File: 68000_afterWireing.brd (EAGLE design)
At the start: 100 x 80 mm, 19 parts, among them IC1 74LS32N, IC2 74LS04N, IC3 74LS04N, X1 22-23-2021

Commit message: Fixed errors and warnings after first autoroute. But Need to move components because their are still airwires after autorouting
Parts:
- removed CLK_OSCILLATOR: ASE, crystal:ASE
- added QG1: SG-615PTW, crystal:SG-615
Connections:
- removed net VSS: 6821_IO.1
- net GND: now also 6821_IO.1, QG1.2; no longer CLK_OSCILLATOR.2
- net N$10: now also MC68000.10
- net N$16: now also D1.A
- net N$26: now also QG1.3
- net N$6: now also 6821_IO.25
- net VCC: now also QG1.4; no longer CLK_OSCILLATOR.4
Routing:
- net GND: track 0.00 -> 343.4 mm, vias 0 -> 9
- net VCC: track 0.00 -> 338.3 mm, vias 0 -> 3
- net A10: track 0.00 -> 207.1 mm, vias 0 -> 8
- net A5: track 0.00 -> 203.2 mm, vias 0 -> 10
- net A9: track 0.00 -> 185.3 mm, vias 0 -> 10
- net D2: track 0.00 -> 184.7 mm, vias 0 -> 5
- net D0: track 0.00 -> 178.2 mm, vias 0 -> 5
- net D1: track 0.00 -> 173.3 mm, vias 0 -> 3
- net A1: track 0.00 -> 171.0 mm, vias 0 -> 5
- net D4: track 0.00 -> 170.2 mm, vias 0 -> 7
- net D5: track 0.00 -> 169.9 mm, vias 0 -> 5
- net A11: track 0.00 -> 166.9 mm, vias 0 -> 10
- net A7: track 0.00 -> 153.5 mm, vias 0 -> 6
- net N$22: track 0.00 -> 150.2 mm, vias 0 -> 4
- net A2: track 0.00 -> 148.7 mm, vias 0 -> 7
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
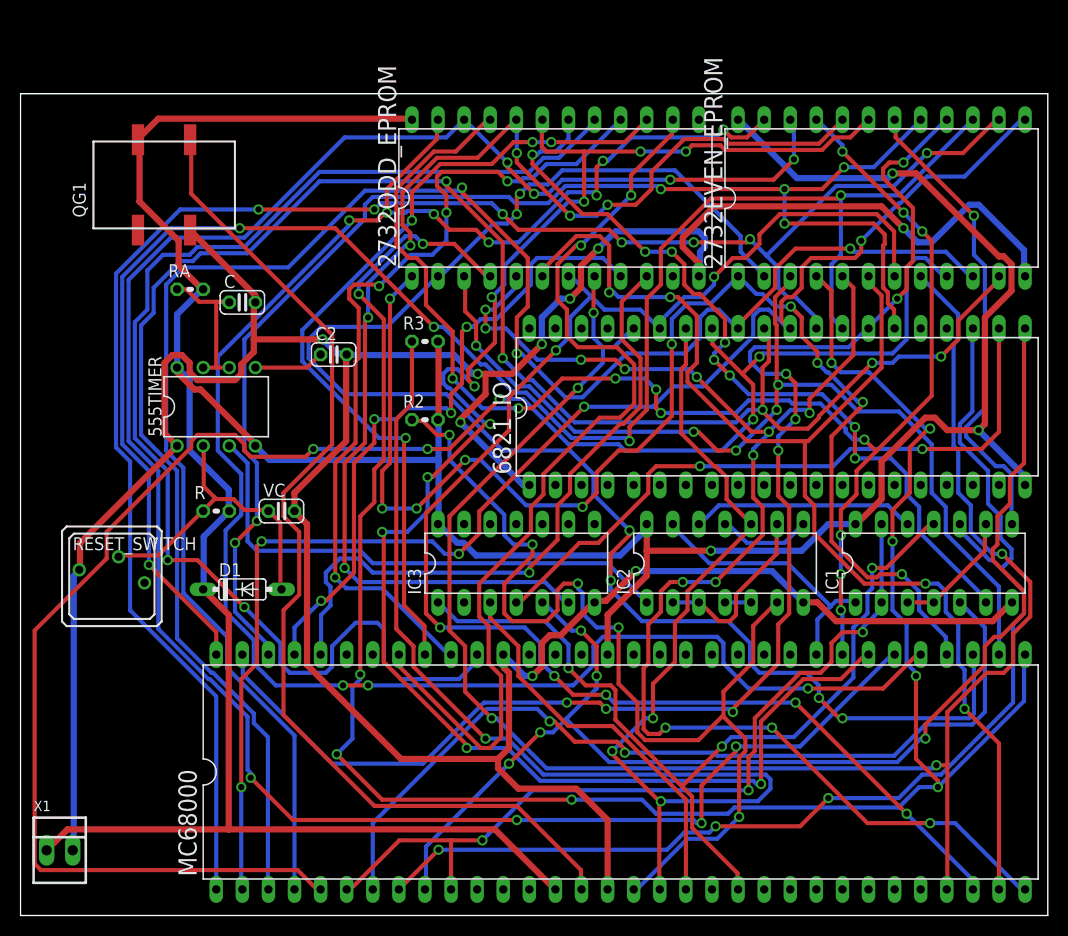
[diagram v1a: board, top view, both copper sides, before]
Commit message: autoroute complete 100% and DRC passed
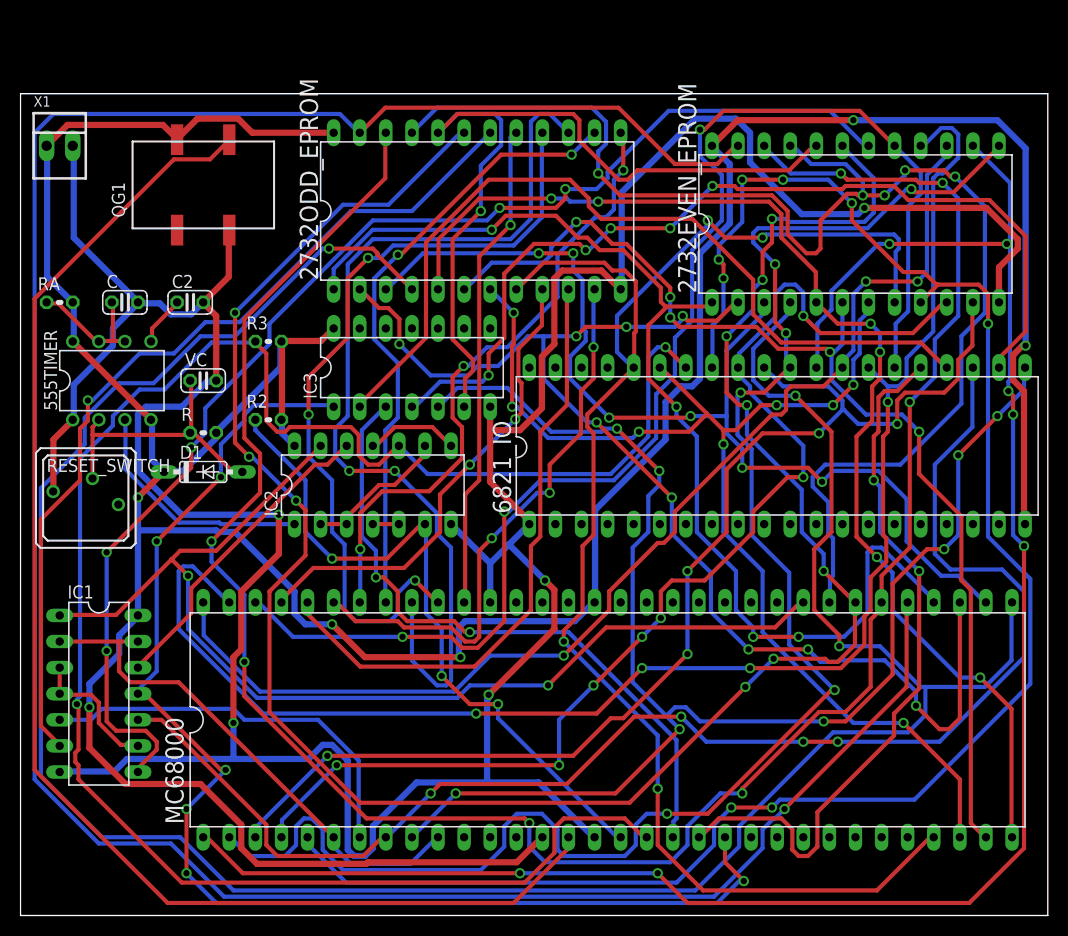
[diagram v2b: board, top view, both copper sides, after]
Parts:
- moved IC1 82.3 mm to (7.62, 21.6), turned to 270 degrees
- moved X1 68.6 mm to (3.81, 74.9)
- moved IC2 35.1 mm to (34.3, 41.9)
- moved IC3 21.6 mm to (38.1, 53.3)
- moved R2 15.2 mm to (24.1, 48.3)
- moved R3 15.2 mm to (24.1, 55.9)
- moved C2 14.9 mm to (16.5, 59.7)
- moved VC 14.8 mm to (17.8, 52.1)
- moved RA 12.8 mm to (3.81, 59.7)
- moved D1 12.0 mm to (17.8, 43.2)
- moved C 11.4 mm to (10.2, 59.7)
- moved 555TIMER 10.5 mm to (8.89, 52.1)
- moved RESET_SWITCH 8.03 mm to (6.35, 40.6)
- moved R 7.73 mm to (17.8, 47.0)
- moved 2732ODD_EPROM 7.73 mm to (44.5, 68.6)
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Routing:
- net N$2: track 0.00 -> 81.9 mm
- net N$3: track 26.9 -> 106.3 mm, vias 0 -> 2
- net N$23: track 46.1 -> 123.9 mm, vias 1 -> 5
- net D15: track 124.3 -> 47.9 mm, vias 2 -> 1
- net N$6: track 0.00 -> 70.5 mm, vias 0 -> 2
- net D2: track 184.7 -> 116.1 mm
- net D11: track 0.00 -> 62.0 mm, vias 0 -> 3
- net A9: track 185.3 -> 244.5 mm, vias 10 -> 1
- net D1: track 173.3 -> 115.2 mm, vias 3 -> 7
- net D5: track 169.9 -> 112.8 mm, vias 5 -> 3
- net D10: track 0.00 -> 55.2 mm, vias 0 -> 3
- net N$8: track 86.2 -> 39.2 mm, vias 2 -> 0
- net A5: track 203.2 -> 245.3 mm, vias 10 -> 3
- net A11: track 166.9 -> 207.3 mm
- net N$5: track 120.3 -> 81.0 mm, vias 6 -> 1
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
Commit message: FINAL: Sent to Bay Area Circuits
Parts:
- removed QG1: SG-615PTW, crystal:SG-615
- added U$1: TTL_OSCILLATOR, TTL_OSCILLATOR:TTL_OSCILLATOR
- renumbered 2732EVEN_EPROM to 2732_ODD, 2732ODD_EPROM to 2732_EVEN, 6821_IO to 6821_ODD
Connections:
- net GND: now also U$1.P$7; no longer QG1.2
- net N$26: now also U$1.P$8; no longer QG1.3
- net VCC: now also MC68000.12, MC68000.13, MC68000.22, MC68000.23, MC68000.24, MC68000.25, U$1.P$14; no longer QG1.4
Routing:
- net A5: track 245.3 -> 111.7 mm
- net A9: track 244.5 -> 115.0 mm, vias 1 -> 5
- net A8: track 109.7 -> 208.4 mm, vias 4 -> 5
- net A3: track 106.9 -> 192.9 mm, vias 5 -> 9
- net D15: track 47.9 -> 132.5 mm, vias 1 -> 7
- net A10: track 214.1 -> 130.6 mm, vias 7 -> 4
- net N$1: track 145.5 -> 212.8 mm, vias 8 -> 3
- net N$11: track 90.2 -> 157.2 mm, vias 5 -> 6
- net N$12: track 64.8 -> 127.9 mm, vias 2 -> 3
- net N$9: track 139.3 -> 198.3 mm, vias 4 -> 5
- net D0: track 173.3 -> 119.1 mm, vias 8 -> 5
- net A6: track 100.6 -> 153.6 mm
- net A11: track 207.3 -> 252.4 mm, vias 10 -> 8
- net D13: track 92.8 -> 52.1 mm, vias 2 -> 0
- net N$3: track 106.3 -> 141.4 mm, vias 2 -> 3
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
